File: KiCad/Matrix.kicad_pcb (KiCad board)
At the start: 2 copper layers, 63.5 x 82.5 mm, 12 parts, among them J1 Conn_01x06_Male, J2 Conn_01x04_Male, J3 Screw_Terminal_01x02, J4 Conn_02x08_Odd_Even, J5 Screw_Terminal_01x02, U1 Lolin32

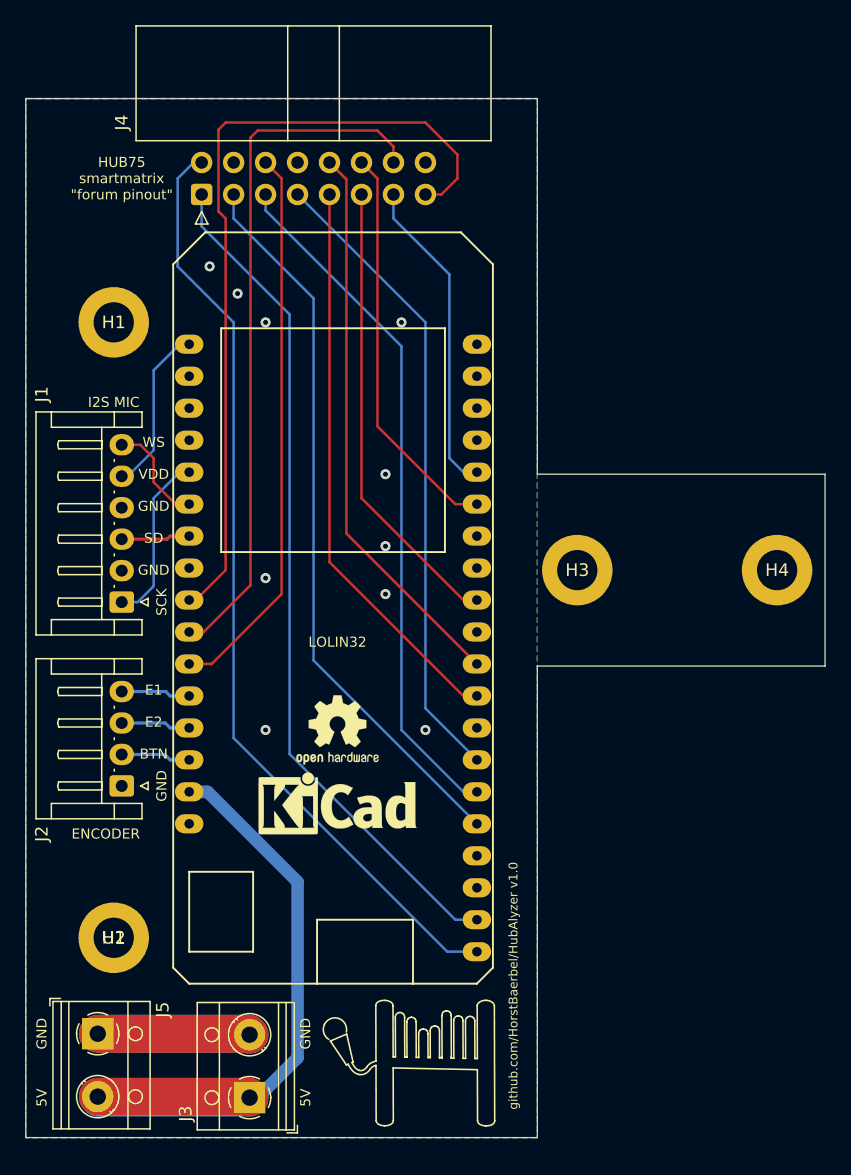
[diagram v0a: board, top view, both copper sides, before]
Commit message: Update board to use E line
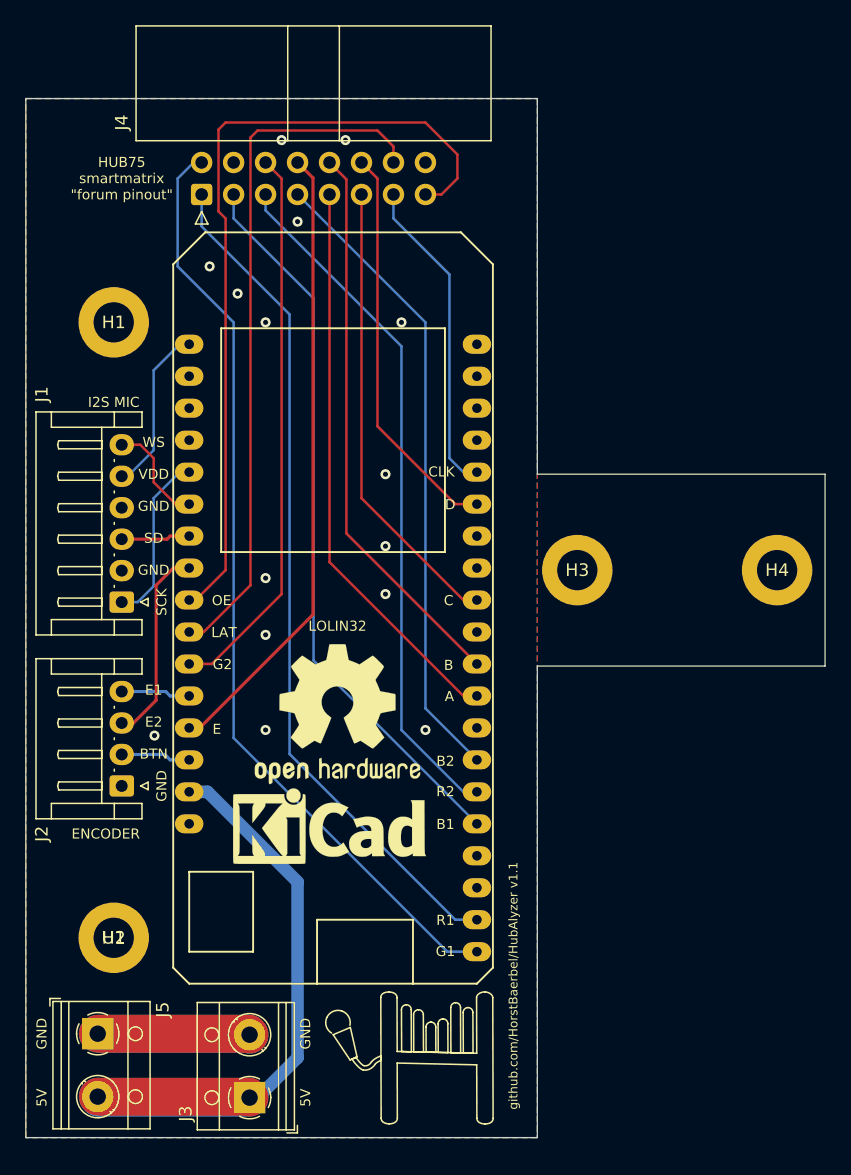
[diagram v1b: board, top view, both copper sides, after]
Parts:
- H5: value MountingHole -> OH logo; footprint Symbol:OSHW-Logo2_7.3x6mm_SilkScreen -> Symbol:OSHW-Logo2_14.6x12mm_SilkScreen
- H6: value MountingHole -> KiCad logo; footprint Symbol:KiCad-Logo_5mm_SilkScreen -> Symbol:KiCad-Logo_6mm_SilkScreen
- moved H6 1.42 mm to (80.6, 101.6)
- moved H5 1.27 mm to (81.3, 92.7)
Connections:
- J4 pad 8: GND -> /E
- U1 pad 13: /E2 -> /E
- U1 pad 8: Net-(U1-Pad8) -> /E2
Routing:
- net /E: track 0.00 -> 50.0 mm
- net /E2: track 5.52 -> 15.8 mm
- net GND: vias 10 -> 15
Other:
- board text added: "A"
- board text added: "B"
- board text added: "B1"
- board text added: "B2"
- board text added: "C"
- board text added: "CLK"
- board text added: "D"
- board text added: "E"
- board text added: "G1"
- board text added: "G2"
- board text added: "LAT"
- board text added: "OE"
- board text added: "R1"
- board text added: "R2"
- board text added: "github.com/HorstBaerbel/HubAlyzer v1.1"
- board text removed: "github.com/HorstBaerbel/HubAlyzer v1.0"
